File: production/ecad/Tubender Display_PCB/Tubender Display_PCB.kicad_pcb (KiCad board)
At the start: 2 copper layers, 2 parts, among them J1 4-1734592-0, J2 4-1734592-0

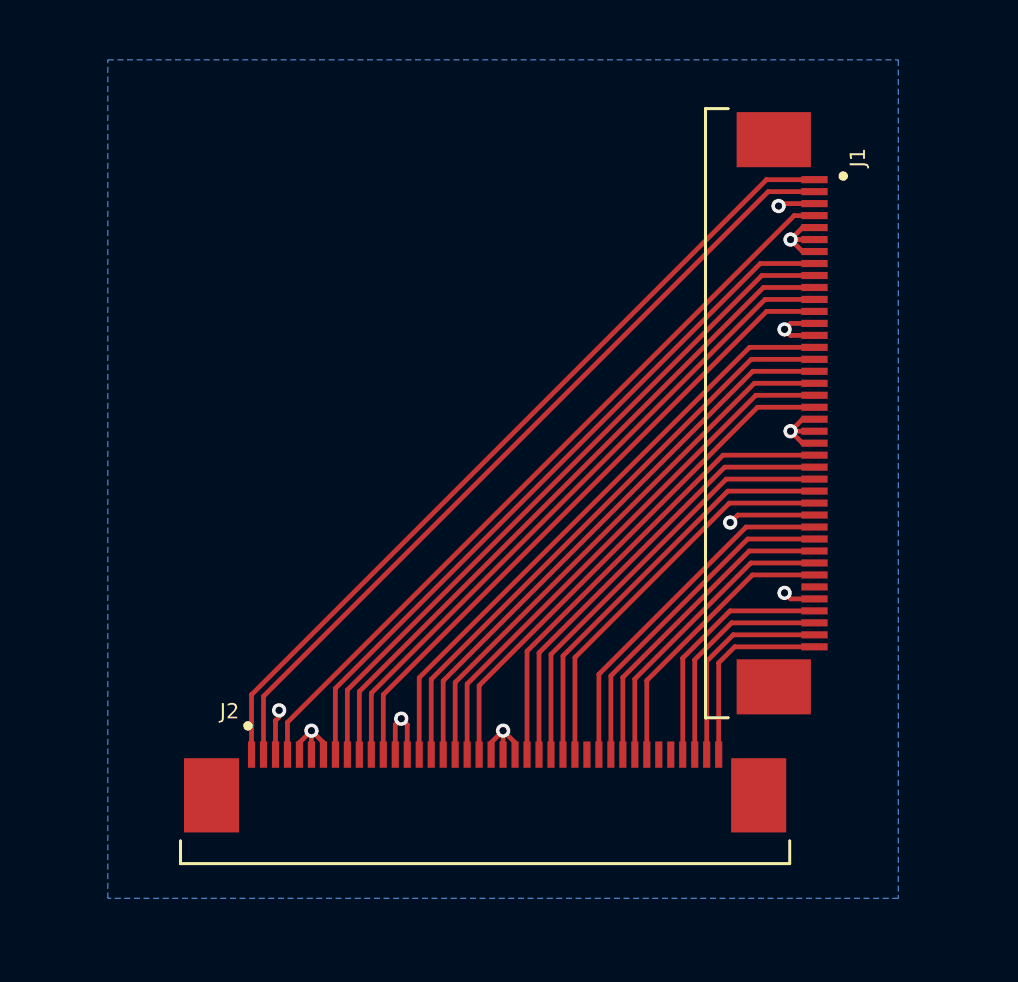
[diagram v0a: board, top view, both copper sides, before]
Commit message: Resolved DRC Erros on connector board
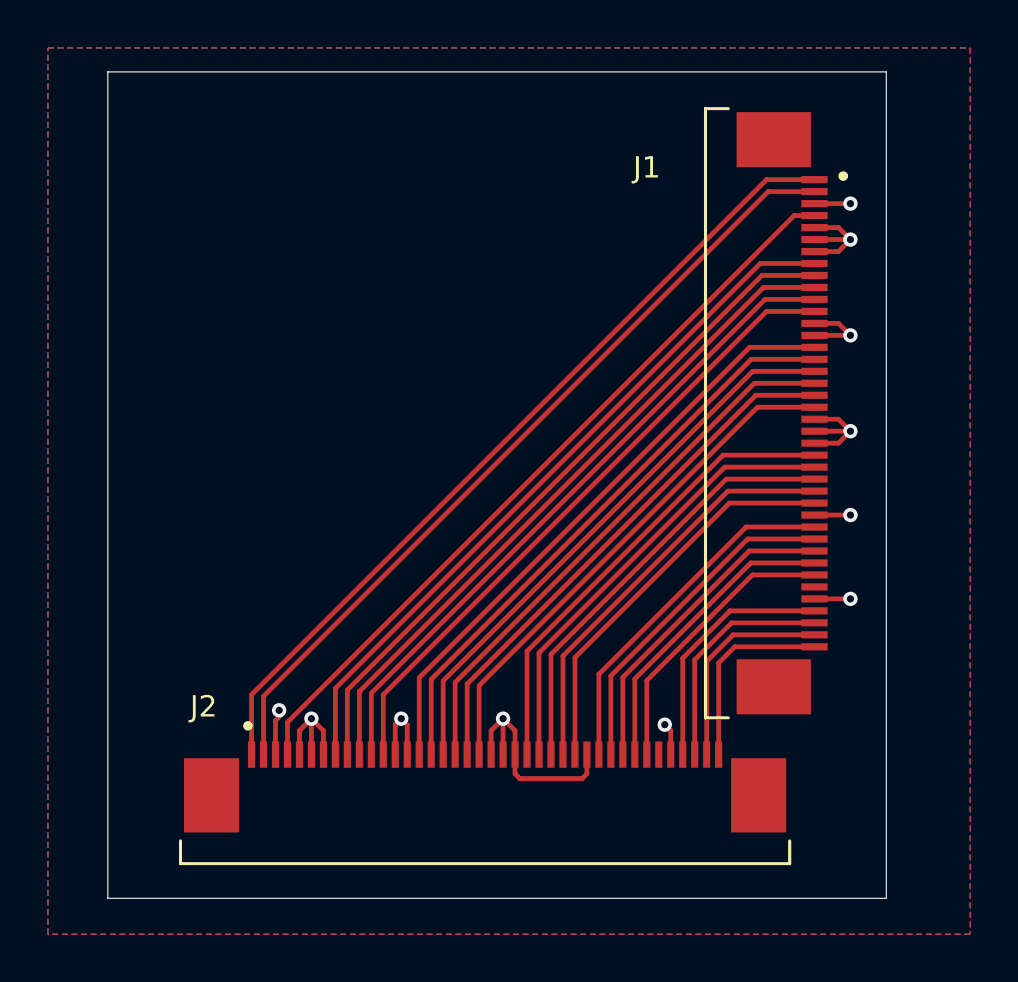
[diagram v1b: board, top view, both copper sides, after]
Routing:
- net GND: track 28.0 -> 38.6 mm, vias 10 -> 11
- added copper zone on F.Cu, net GND
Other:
- board outline added: 32.5 x 34.5 mm

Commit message: Revert "okay"
This reverts commit a5d04aacf17b2a0e1fddfefa2daa114170fce467, reversing
changes made to 85b8c41c143529192f5821f916a37eef7153b122.
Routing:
- net GND: track 38.6 -> 28.0 mm, vias 11 -> 10
- removed copper zone on F.Cu, net GND
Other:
- board outline removed
